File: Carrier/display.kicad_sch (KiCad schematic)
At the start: 16 parts, among them J9 Conn_01x30, Q2 AO3400A, U16 AP3032, U3 AMS1117-1.8

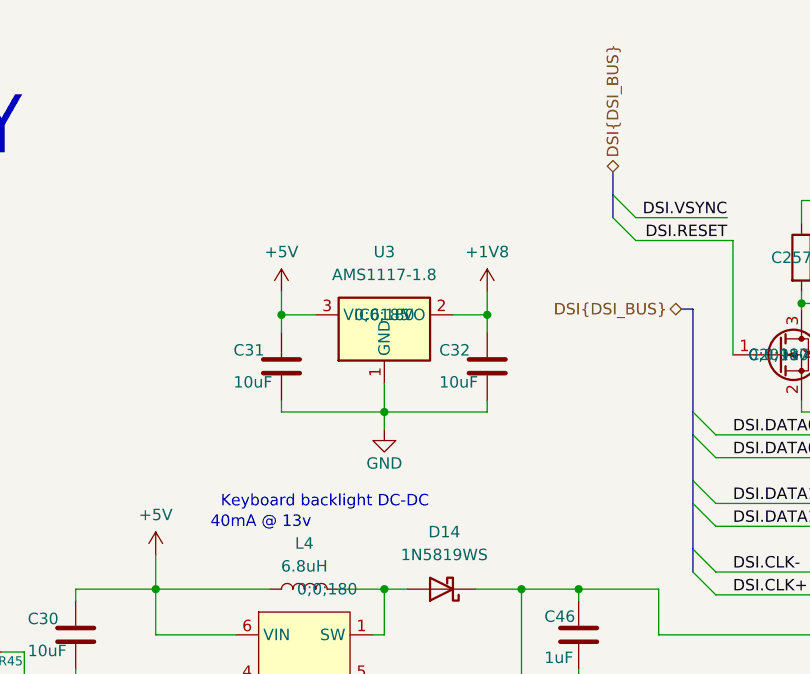
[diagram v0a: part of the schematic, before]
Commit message: fix: sync schematic prot3 and v2.5
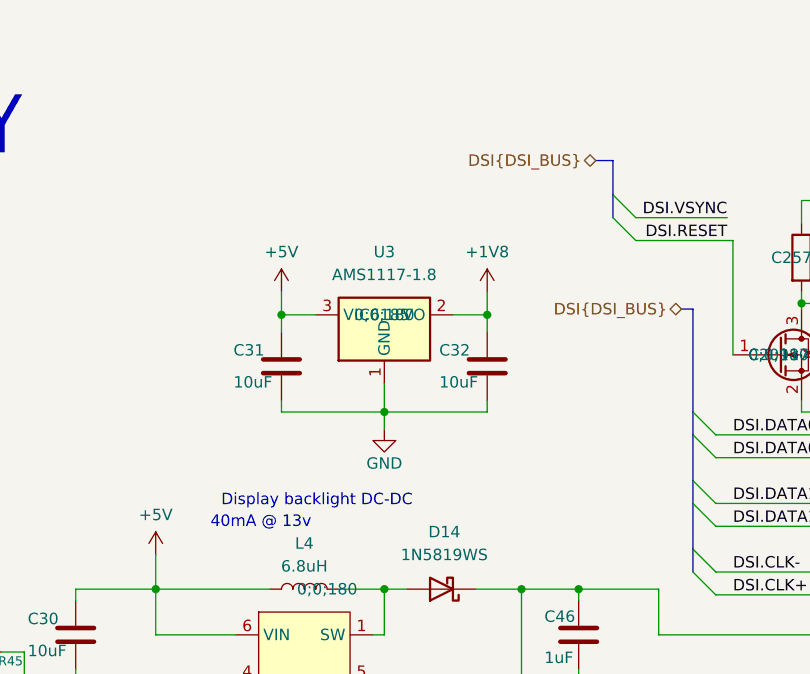
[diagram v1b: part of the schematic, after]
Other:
- note added: "Display backlight DC-DC"
- note removed: "Keyboard backlight DC-DC"
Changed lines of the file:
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@@
 		)
 	)
-	(text "Keyboard backlight DC-DC"
+	(text "Display backlight DC-DC"
 		(exclude_from_sim no)
-		(at 93.091 60.833 0)
+		(at 92.202 60.706 0)
 		(effects
 			(font
@@
 		)
 	)
+	(bus
+		(pts
+			(xy 125.095 22.86) (xy 125.095 26.67)
+		)
+		(stroke
+			(width 0)
+			(type default)
+		)
+	)
 	(wire
 		(pts
@@
 		)
 	)
+	(bus
+		(pts
+			(xy 123.19 22.86) (xy 125.095 22.86)
+		)
+		(stroke
+			(width 0)
+			(type default)
+		)
+	)
 	(wire
 		(pts
@@
 		(pts
 			(xy 146.05 50.8) (xy 174.625 50.8)
-		)
-		(stroke
-			(width 0)
-			(type default)
-		)
-	)
-	(bus
-		(pts
-			(xy 125.095 26.67) (xy 125.095 24.13)
 		)
 		(stroke
@@
 	(hierarchical_label "DSI{DSI_BUS}"
 		(shape bidirectional)
-		(at 125.095 24.13 90)
+		(at 123.19 22.86 180)
 		(effects
 			(font
 				(size 1.27 1.27)
 			)
-			(justify left)
-		)
-	)
+			(justify right)
+		)
+	)

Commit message: chore: repo cleanup
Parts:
- removed R45: 0R, Resistor_SMD:R_0603_1608Metric, symbol Device:R_Small
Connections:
- net ADJ_BL_KEYBOARD_DISPLAY renamed BL_PWM
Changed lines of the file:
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@@
-	)
-	(junction
-		(at 59.69 80.645)
-		(diameter 0)
-		(color 0 0 0 0)
 	)
 	(junction
@@
 	(wire
 		(pts
-			(xy 49.53 80.645) (xy 59.69 80.645)
-		)
-		(stroke
-			(width 0)
-			(type default)
-		)
-	)
-	(wire
-		(pts
 			(xy 107.315 40.005) (xy 111.125 40.005)
 		)
@@
 	(wire
 		(pts
-			(xy 57.15 77.47) (xy 59.69 77.47)
-		)
-		(stroke
-			(width 0)
-			(type default)
-		)
-	)
-	(wire
-		(pts
 			(xy 174.625 81.28) (xy 174.625 83.82)
 		)
@@
 	(wire
 		(pts
+			(xy 59.69 80.01) (xy 59.69 80.645)
+		)
+		(stroke
+			(width 0)
+			(type default)
+		)
+	)
+	(wire
+		(pts
 			(xy 174.625 73.66) (xy 177.165 73.66)
 		)
@@
 	(wire
 		(pts
+			(xy 49.53 80.01) (xy 59.69 80.01)
+		)
+		(stroke
+			(width 0)
+			(type default)
+		)
+	)
+	(wire
+		(pts
 			(xy 111.125 49.53) (xy 111.125 50.8)
 		)
@@
 	(wire
 		(pts
-			(xy 49.53 77.47) (xy 52.07 77.47)
-		)
-		(stroke
-			(width 0)
-			(type default)
-		)
-	)
-	(wire
-		(pts
 			(xy 99.695 70.485) (xy 102.235 70.485)
 		)
@@
 		(pts
 			(xy 177.165 22.86) (xy 174.625 22.86)
-		)
-		(stroke
-			(width 0)
-			(type default)
-		)
-	)
-	(wire
-		(pts
-			(xy 59.69 77.47) (xy 59.69 80.645)
 		)
 		(stroke
@@
 			)
 			(justify left bottom)
-		)
-	)
-	(hierarchical_label "ADJ_BL_KEYBOARD_DISPLAY"
-		(shape bidirectional)
-		(at 49.53 80.645 180)
-		(effects
-			(font
-				(size 1.27 1.27)
-			)
-			(justify right)
 		)
 	)
@@
 		)
 	)
-	(hierarchical_label "ADJ_BL"
-		(shape bidirectional)
-		(at 49.53 77.47 180)
+	(hierarchical_label "BL_PWM"
+		(shape input)
+		(at 49.53 80.01 180)
 		(effects
 			(font
@@
 					(unit 1)
 				)
-			)
-		)
-	)
-	(symbol
-		(lib_id "Device:R_Small")
-		(at 54.61 77.47 270)
-		(unit 1)
-		(exclude_from_sim no)
-		(in_bom yes)
-		(on_board yes)
-		(dnp no)
-		(property "Reference" "R45"
-			(at 58.166 78.486 90)
-			(effects
-				(font
-					(size 1.016 1.016)
-				)
-			)
-		)
-		(property "Value" "0R"
-			(at 51.054 78.486 90)
-			(effects
-				(font
-					(size 1.27 1.27)
-				)
-			)
-		)
-		(property "Footprint" "Resistor_SMD:R_0603_1608Metric"
-			(at 54.61 77.47 0)
-			(effects
-				(font
-					(size 1.27 1.27)
-				)
-				(hide yes)
-			)
-		)
-		(property "Datasheet" "~"
-			(at 54.61 77.47 0)
-			(effects
-				(font
-					(size 1.27 1.27)
-				)
-				(hide yes)
-			)
-		)
-		(property "Description" "Resistor, small symbol"
-			(at 54.61 77.47 0)
-			(effects
-				(font
-					(size 1.27 1.27)
-				)
-				(hide yes)
-			)
-		)
-		(property "Sim.Device" ""
-			(at 54.61 77.47 0)
-			(effects
-				(font
-					(size 1.27 1.27)
-				)
-			)
-		)
-		(property "LCSC" "C15402"
-			(at 54.61 77.47 0)
-			(effects
-				(font
-					(size 1.27 1.27)
-				)
-				(hide yes)
-			)
-		)
-		(property "DigiKey_Part_Number" ""
-			(at 54.61 77.47 0)
-			(effects
-				(font
-					(size 1.27 1.27)
-				)
-			)
-		)
-		(property "Sim.Pin" ""
-			(at 54.61 77.47 0)
-			(effects
-				(font
-					(size 1.27 1.27)
-				)
-			)
-		)
-		(property "JLCPCB_CORRECTION" ""
-			(at 54.61 77.47 0)
-			(effects
-				(font
-					(size 1.27 1.27)
-				)
-			)
-		)
-		(property "Purchase-URL" ""
-			(at 54.61 77.47 90)
-			(effects
-				(font
-					(size 1.27 1.27)
-				)
-				(hide yes)
-			)
-		)
-		(pin "1"
-		)
-		(pin "2"
-		)
-		(instances
-			(project "badgeCarrierCard"
-				(path "/d0a98fce-b133-4503-8f8a-83b2a1eed591/bde3e5bf-8f05-407f-8448-d7dad1501e9c"
-					(reference "R45")
-					(unit 1)
-				)

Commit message: chore: lib cleanup
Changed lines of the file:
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@@
-	)
-	(bus_entry
-		(at 127.635 31.75)
-		(size -2.54 -2.54)
-		(stroke
-			(width 0)
-			(type default)
-		)
 	)
 	(bus_entry
@@
 	)
 	(bus_entry
+		(at 133.985 41.91)
+		(size 2.54 2.54)
+		(stroke
+			(width 0)
+			(type default)
+		)
+	)
+	(bus_entry
 		(at 133.985 60.96)
 		(size 2.54 2.54)
@@
 		)
 	)
-	(bus_entry
-		(at 127.635 29.21)
-		(size -2.54 -2.54)
-		(stroke
-			(width 0)
-			(type default)
-		)
-	)
 	(wire
 		(pts
@@
 	(wire
 		(pts
-			(xy 127.635 29.21) (xy 137.795 29.21)
-		)
-		(stroke
-			(width 0)
-			(type default)
-		)
-	)
-	(wire
-		(pts
 			(xy 174.625 78.74) (xy 177.165 78.74)
 		)
@@
 		)
 	)
+	(wire
+		(pts
+			(xy 146.05 49.53) (xy 146.05 50.8)
+		)
+		(stroke
+			(width 0)
+			(type default)
+		)
+	)
+	(wire
+		(pts
+			(xy 177.165 93.98) (xy 177.165 96.52)
+		)
+		(stroke
+			(width 0)
+			(type default)
+		)
+	)
+	(wire
+		(pts
+			(xy 167.005 40.64) (xy 167.005 78.105)
+		)
+		(stroke
+			(width 0)
+			(type default)
+		)
+	)
+	(wire
+		(pts
+			(xy 131.445 85.725) (xy 139.7 85.725)
+		)
+		(stroke
+			(width 0)
+			(type default)
+		)
+	)
+	(wire
+		(pts
+			(xy 99.695 50.8) (xy 99.695 47.625)
+		)
+		(stroke
+			(width 0)
+			(type default)
+		)
+	)
+	(wire
+		(pts
+			(xy 49.53 80.01) (xy 59.69 80.01)
+		)
+		(stroke
+			(width 0)
+			(type default)
+		)
+	)
+	(wire
+		(pts
+			(xy 111.125 49.53) (xy 111.125 50.8)
+		)
+		(stroke
+			(width 0)
+			(type default)
+		)
+	)
+	(wire
+		(pts
+			(xy 65.405 79.375) (xy 65.405 94.615)
+		)
+		(stroke
+			(width 0)
+			(type default)
+		)
+	)
+	(wire
+		(pts
+			(xy 160.655 33.02) (xy 160.655 36.83)
+		)
+		(stroke
+			(width 0)
+			(type default)
+		)
+	)
 	(bus
 		(pts
-			(xy 125.095 22.86) (xy 125.095 26.67)
-		)
-		(stroke
-			(width 0)
-			(type default)
-		)
-	)
-	(wire
-		(pts
-			(xy 146.05 49.53) (xy 146.05 50.8)
-		)
-		(stroke
-			(width 0)
-			(type default)
-		)
-	)
-	(wire
-		(pts
-			(xy 177.165 93.98) (xy 177.165 96.52)
-		)
-		(stroke
-			(width 0)
-			(type default)
-		)
-	)
-	(wire
-		(pts
-			(xy 167.005 40.64) (xy 167.005 78.105)
-		)
-		(stroke
-			(width 0)
-			(type default)
-		)
-	)
-	(wire
-		(pts
-			(xy 131.445 85.725) (xy 139.7 85.725)
-		)
-		(stroke
-			(width 0)
-			(type default)
-		)
-	)
-	(wire
-		(pts
-			(xy 99.695 50.8) (xy 99.695 47.625)
-		)
-		(stroke
-			(width 0)
-			(type default)
-		)
-	)
-	(wire
-		(pts
-			(xy 49.53 80.01) (xy 59.69 80.01)
-		)
-		(stroke
-			(width 0)
-			(type default)
-		)
-	)
-	(wire
-		(pts
-			(xy 111.125 49.53) (xy 111.125 50.8)
-		)
-		(stroke
-			(width 0)
-			(type default)
-		)
-	)
-	(wire
-		(pts
-			(xy 65.405 79.375) (xy 65.405 94.615)
-		)
-		(stroke
-			(width 0)
-			(type default)
-		)
-	)
-	(wire
-		(pts
-			(xy 160.655 33.02) (xy 160.655 36.83)
+			(xy 133.985 39.37) (xy 133.985 41.91)
 		)
 		(stroke
@@
 	(bus
 		(pts
-			(xy 133.985 39.37) (xy 133.985 50.8)
+			(xy 133.985 41.91) (xy 133.985 50.8)
 		)
 		(stroke
@@
 	(wire
 		(pts
-			(xy 127.635 31.75) (xy 138.43 31.75)
-		)
-		(stroke
-			(width 0)
-			(type default)
-		)
-	)
-	(wire
-		(pts
 			(xy 74.295 70.485) (xy 86.995 70.485)
 		)
@@
 	(wire
 		(pts
-			(xy 138.43 31.75) (xy 138.43 44.45)
-		)
-		(stroke
-			(width 0)
-			(type default)
-		)
-	)
-	(wire
-		(pts
 			(xy 177.165 22.86) (xy 174.625 22.86)
 		)
@@
 		)
 	)
-	(bus
-		(pts
-			(xy 123.19 22.86) (xy 125.095 22.86)
-		)
-		(stroke
-			(width 0)
-			(type default)
-		)
-	)
 	(wire
 		(pts
@@
 		)
 	)
-	(bus
-		(pts
-			(xy 125.095 29.21) (xy 125.095 26.67)
-		)
-		(stroke
-			(width 0)
-			(type default)
-		)
-	)
 	(wire
 		(pts
@@
 		(pts
 			(xy 157.48 38.735) (xy 157.48 48.26)
+		)
+		(stroke
+			(width 0)
+			(type default)
+		)
+	)
+	(wire
+		(pts
+			(xy 136.525 44.45) (xy 138.43 44.45)
 		)
 		(stroke
@@
 		)
 	)
-	(label "DSI.VSYNC"
-		(at 137.795 29.21 180)
+	(label "DSI.RESET"
+		(at 138.43 44.45 90)
 		(effects
 			(font
 				(size 1.27 1.27)
 			)
-			(justify right bottom)
+			(justify left bottom)
 		)
 	)
@@
 		)
 	)
-	(label "DSI.RESET"
-		(at 137.795 31.75 180)
-		(effects
-			(font
-				(size 1.27 1.27)
-			)
-			(justify right bottom)
-		)
-	)
 	(label "DSI.DATA0-"
 		(at 138.43 53.34 0)
@@
 		)
 	)
-	(hierarchical_label "DSI{DSI_BUS}"
-		(shape bidirectional)
-		(at 123.19 22.86 180)
-		(effects
-			(font
-				(size 1.27 1.27)
-			)
-			(justify right)
-		)
-	)

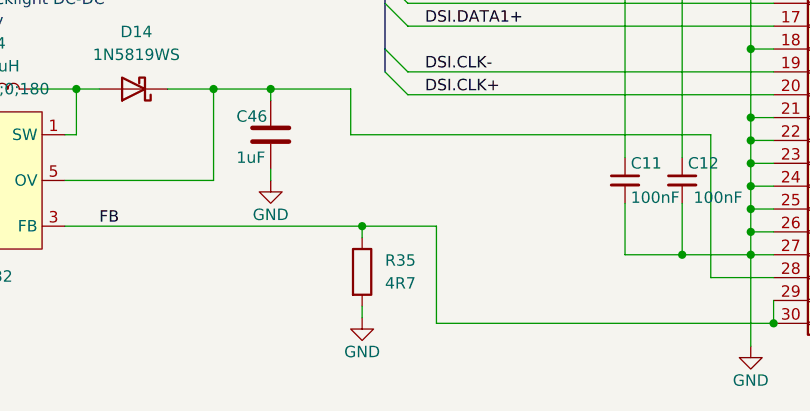
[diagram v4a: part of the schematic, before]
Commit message: norun: fix: change disp. backlight feedback resistance
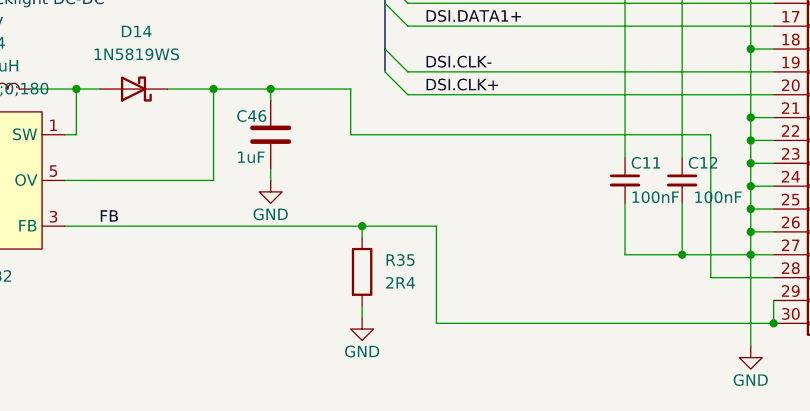
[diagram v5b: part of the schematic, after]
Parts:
- R35: value 4R7 -> 2R4; LCSC C25121 -> C166486
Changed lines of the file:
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@@
 			)
 		)
-		(property "Value" "4R7"
+		(property "Value" "2R4"
 			(at 133.985 92.0749 0)
 			(effects
@@
 			)
 		)
-		(property "LCSC" "C25121"
+		(property "LCSC" "C166486"
 			(at 131.445 90.805 0)
 			(effects
